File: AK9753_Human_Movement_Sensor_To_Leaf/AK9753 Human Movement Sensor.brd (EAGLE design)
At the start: 25.4 x 25.4 mm, 9 parts, among them J3 PTH, U2 AK9753

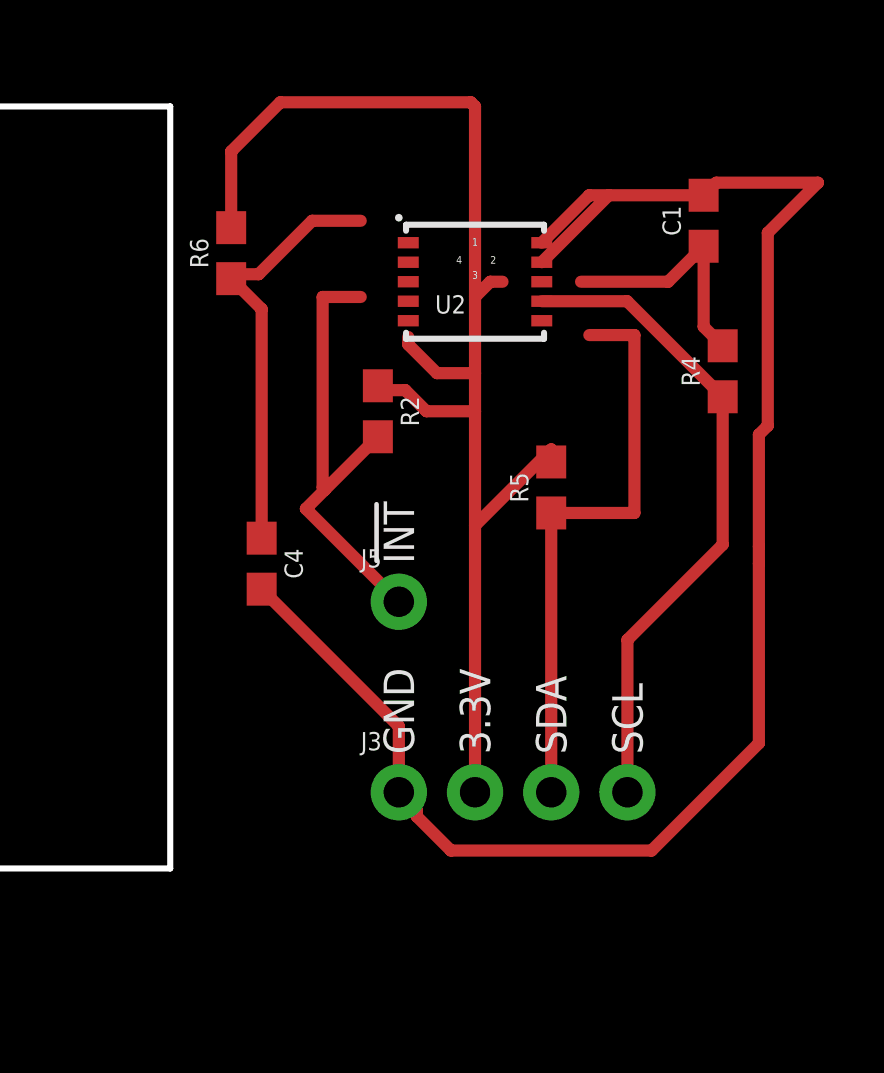
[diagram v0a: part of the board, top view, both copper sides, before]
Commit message: Finished schematic
drawing board next
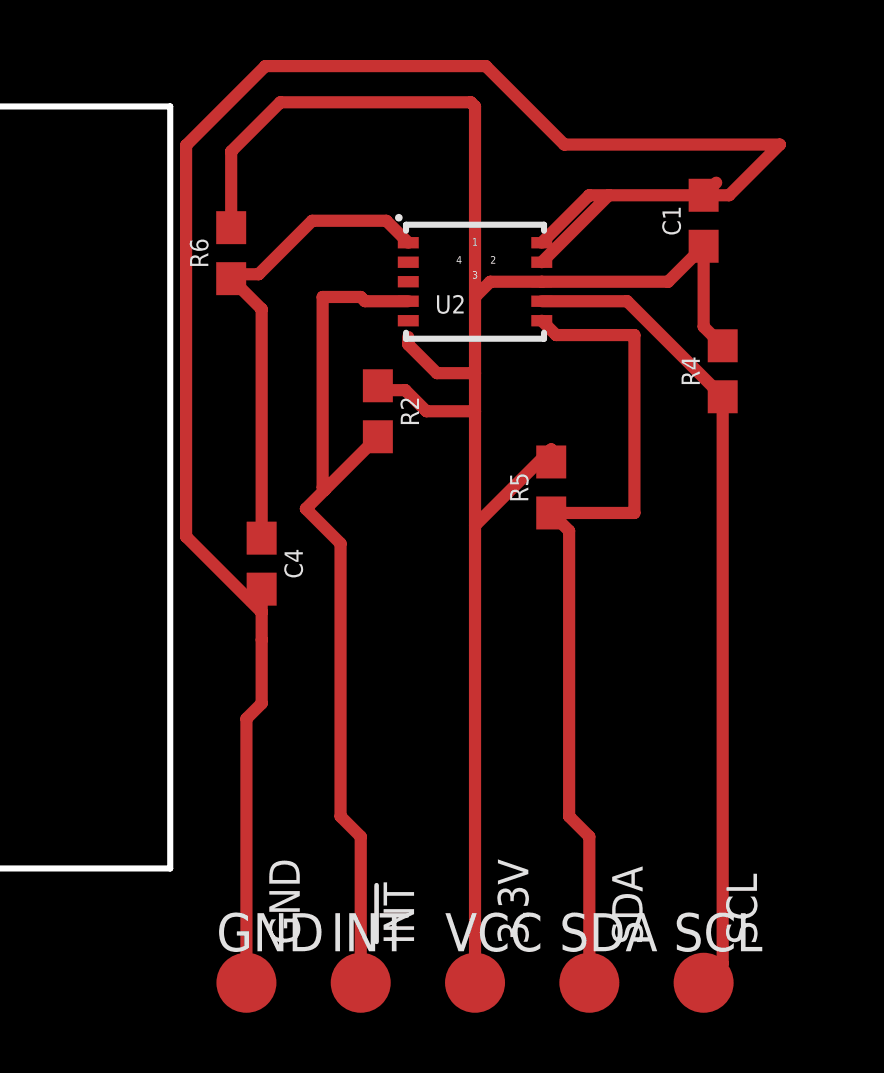
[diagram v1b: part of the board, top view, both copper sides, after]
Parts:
- removed J3: PTH, SparkFun-Connectors:1X04_NO_SILK
- removed J5: (no value), SparkFun-Connectors:1X01_NO_SILK
- added GND, INT, SCL, SDA, VCC: TPSQTP20R, testpad:TP20R
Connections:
- net !INT: now also INT.TP; no longer J5.1
- net 3.3V: now also VCC.TP; no longer J3.2
- net GND: now also GND.TP; no longer J3.1
- net SCL: now also SCL.TP; no longer J3.4
- net SDA: now also SDA.TP; no longer J3.3
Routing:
- net !INT: track 15.5 -> 29.3 mm
- net GND: track 55.8 -> 64.9 mm
- net 3.3V: track 54.5 -> 63.5 mm
- net SDA: track 19.5 -> 28.2 mm
- net SCL: track 21.8 -> 27.1 mm
- net VDD: track 14.2 -> 16.1 mm

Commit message: Leaf outline done
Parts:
- moved C1 46.0 mm to (12.2, 55.6)
- moved C4 46.0 mm to (-2.55, 44.2)
- moved GND 46.0 mm to (-3.06, 30.2)
- moved INT 46.0 mm to (0.75, 30.2)
- moved R2 46.0 mm to (1.32, 49.2)
- moved R4 46.0 mm to (12.8, 50.6)
- moved R5 46.0 mm to (7.10, 46.7)
- moved R6 46.0 mm to (-3.57, 54.5)
- moved SCL 46.0 mm to (12.2, 30.2)
- moved SDA 46.0 mm to (8.37, 30.2)
- moved U2 46.0 mm to (4.56, 53.6)
- moved VCC 46.0 mm to (4.56, 30.2)
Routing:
- removed copper zone on layer 1, net GND
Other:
- board size 25.4 x 25.4 mm -> 76.2 x 71 mm

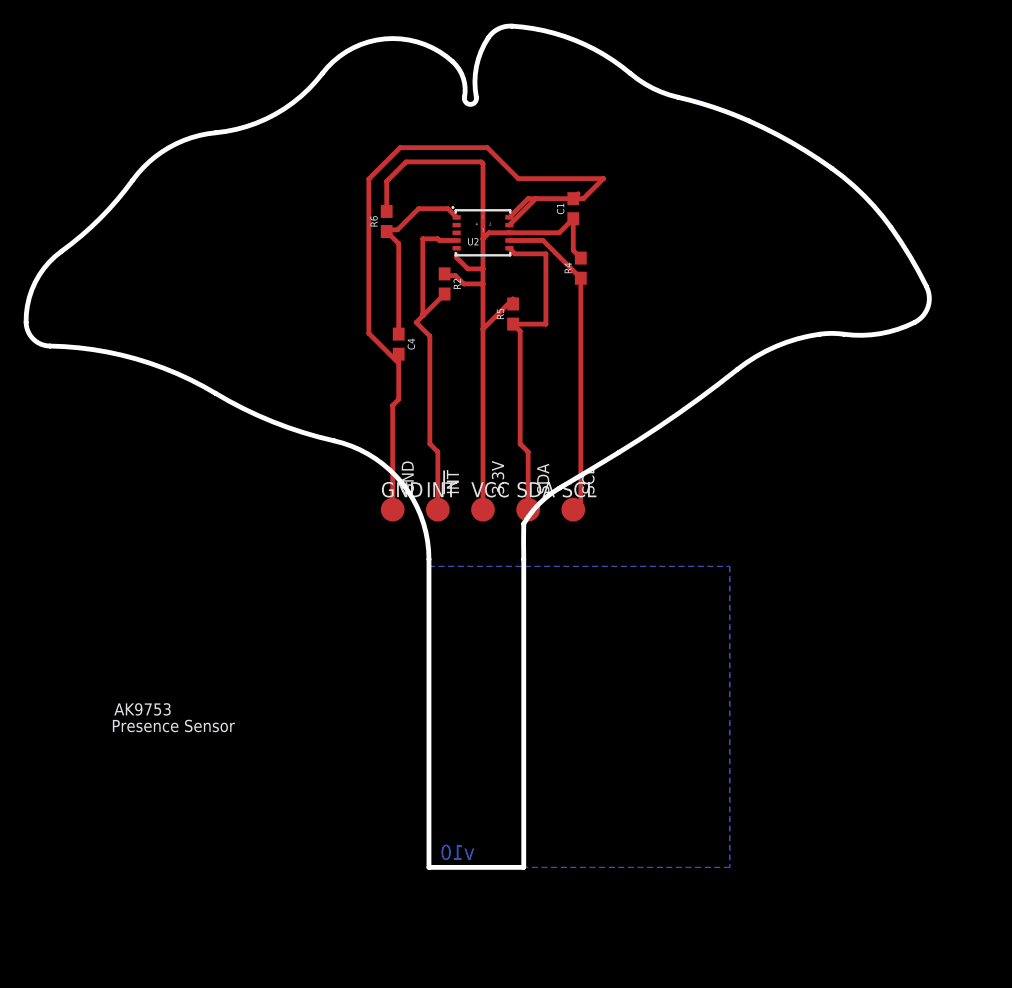
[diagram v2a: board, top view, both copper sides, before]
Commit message: Leaf structure done
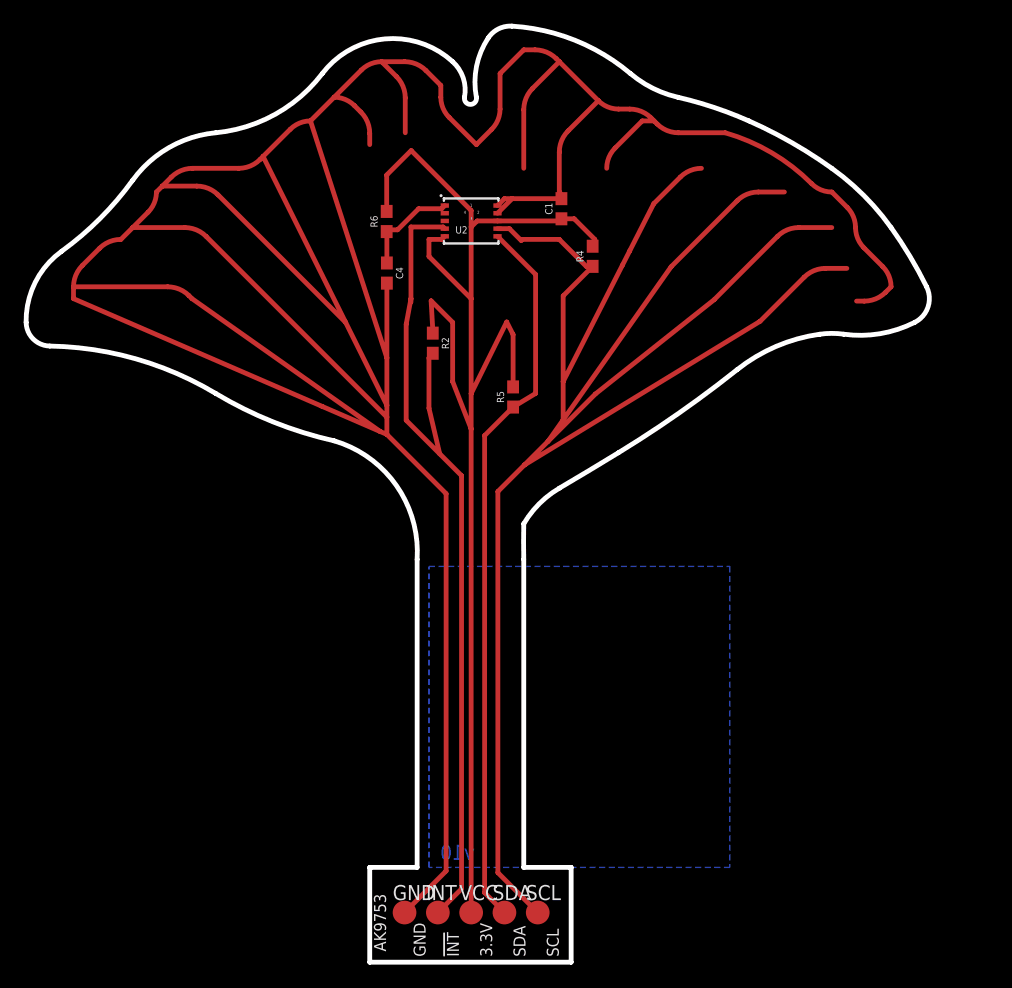
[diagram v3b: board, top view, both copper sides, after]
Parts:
- moved SCL 34.1 mm to (9.18, -3.81)
- moved SDA 34.1 mm to (6.37, -3.81)
- moved GND 34.0 mm to (-2.06, -3.81)
- moved VCC 34.0 mm to (3.56, -3.81)
- moved INT 34.0 mm to (0.75, -3.81)
- moved R5 7.00 mm to (7.10, 39.7)
- moved C4 6.08 mm to (-3.55, 50.2)
- moved R2 5.10 mm to (0.32, 44.2)
- moved R4 1.41 mm to (13.8, 51.6)
- moved U2 1.41 mm to (3.56, 54.6)
- moved C1 1.00 mm to (11.2, 55.6)
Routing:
- net GND: track 64.9 -> 351.6 mm
- net SCL: track 27.1 -> 181.4 mm
- net 3.3V: track 63.5 -> 119.6 mm
- net !INT: track 29.3 -> 72.6 mm
- net SDA: track 28.2 -> 61.2 mm
- net VDD: track 16.1 -> 8.47 mm
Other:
- board size 76.2 x 71 mm -> 76.2 x 79 mm

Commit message: small changes
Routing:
- net !INT: track 72.6 -> 71.4 mm
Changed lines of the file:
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@@
 <contactref element="R4" pad="1"/>
 <contactref element="U2" pad="4"/>
-<wire x1="5.785" y1="53.908" x2="6.785" y2="53.908" width="0.4064" layer="1"/>
-<wire x1="7.785" y1="52.908" x2="6.785" y2="53.908" width="0.4064" layer="1"/>
+<wire x1="5.785" y1="53.908" x2="7.092" y2="53.908" width="0.4064" layer="1"/>
 <contactref element="SCL" pad="TP"/>
 <wire x1="14.04575" y1="39.95425" x2="10.04575" y2="35.95425" width="0.4064" layer="1"/>
@@
 <wire x1="8.04575" y1="33.95425" x2="27.945853125" y2="46.088796875" width="0.4064" layer="1"/>
 <wire x1="14.04575" y1="39.95425" x2="24.0701875" y2="47.911578125" width="0.4064" layer="1"/>
-<wire x1="13.815" y1="50.7235" x2="13.2765" y2="50.7235" width="0.4064" layer="1"/>
-<wire x1="13.2765" y1="50.7235" x2="11" y2="53" width="0.4064" layer="1"/>
-<wire x1="11" y1="53" x2="7.877" y2="53" width="0.4064" layer="1"/>
-<wire x1="7.877" y1="53" x2="7.785" y2="52.908" width="0.4064" layer="1"/>
+<wire x1="10.2765" y1="50.7235" x2="13.815" y2="50.7235" width="0.4064" layer="1"/>
 <wire x1="10.04575" y1="35.95425" x2="11.326071875" y2="37.77009375" width="0.4064" layer="1"/>
 <wire x1="20.437" y1="50.691878125" x2="11.326071875" y2="37.77009375" width="0.4064" layer="1"/>
@@
 <wire x1="31.668609375" y1="49.811553125" x2="33.4646625" y2="50.555503125" width="0.4064" layer="1" curve="-45"/>
 <wire x1="33.4646625" y1="50.555503125" x2="35.27104375" y2="50.555503125" width="0.4064" layer="1"/>
+<wire x1="7.092" y1="53.908" x2="10.2765" y2="50.7235" width="0.4064" layer="1"/>
 </signal>
 <signal name="SDA">
@@
 <contactref element="U2" pad="7"/>
 <contactref element="R2" pad="2"/>
-<wire x1="-1.52" y1="54.05" x2="-1.52" y2="48" width="0.4064" layer="1"/>
 <contactref element="INT" pad="TP"/>
-<wire x1="-1.52" y1="48" x2="-1.52" y2="47.7" width="0.4064" layer="1"/>
 <wire x1="-1.923" y1="37.73518125" x2="0.906090625" y2="34.906090625" width="0.4064" layer="1"/>
 <wire x1="0.906090625" y1="34.906090625" x2="2.75" y2="33.06218125" width="0.4064" layer="1"/>
 <wire x1="2.75" y1="33.06218125" x2="2.75" y2="-1.81" width="0.4064" layer="1"/>
 <wire x1="2.75" y1="-1.81" x2="0.75" y2="-3.81" width="0.4064" layer="1"/>
-<wire x1="-1.923" y1="45.833" x2="-1.923" y2="37.73518125" width="0.4064" layer="1"/>
-<wire x1="1.335" y1="53.908" x2="1.193" y2="54.05" width="0.4064" layer="1"/>
-<wire x1="1.193" y1="54.05" x2="-1.52" y2="54.05" width="0.4064" layer="1"/>
-<wire x1="-1.52" y1="48" x2="-1.923" y2="45.833" width="0.4064" layer="1"/>
+<wire x1="-1.923" y1="52.077" x2="-1.923" y2="37.73518125" width="0.4064" layer="1"/>
 <wire x1="0.906090625" y1="34.906090625" x2="0" y2="38.753659375" width="0.4064" layer="1"/>
 <wire x1="0" y1="38.753659375" x2="0" y2="43" width="0.4064" layer="1"/>
 <wire x1="0" y1="43" x2="0.3215" y2="43.39" width="0.4064" layer="1"/>
+<wire x1="1.335" y1="53.908" x2="-0.092" y2="53.908" width="0.4064" layer="1"/>
+<wire x1="-0.092" y1="53.908" x2="-1.923" y2="52.077" width="0.4064" layer="1"/>
 </signal>
 <signal name="ADR0">
@@
 <wire x1="-3.568" y1="53.6605" x2="-3.4212" y2="53.8073" width="0.4064" layer="1"/>
 <wire x1="-3.4212" y1="53.8073" x2="-2.6524625" y2="53.8073" width="0.4064" layer="1"/>
-<wire x1="-2.6524625" y1="53.8073" x2="-0.8697625" y2="55.59" width="0.4064" layer="1"/>
-<wire x1="1.067" y1="55.59" x2="1.335" y2="55.858" width="0.4064" layer="1"/>
-<wire x1="-0.8697625" y1="55.59" x2="1.067" y2="55.59" width="0.4064" layer="1"/>
+<wire x1="-0.6017625" y1="55.858" x2="1.335" y2="55.858" width="0.4064" layer="1"/>
+<wire x1="-2.6524625" y1="53.8073" x2="-0.6017625" y2="55.858" width="0.4064" layer="1"/>
 </signal>
 </signals>
